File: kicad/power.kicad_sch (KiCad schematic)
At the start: 1 part, among them J1 1726480105

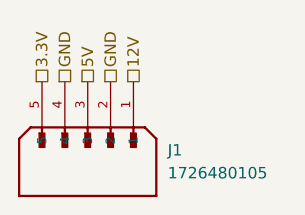
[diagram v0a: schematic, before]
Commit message: finished circuits for rp2040
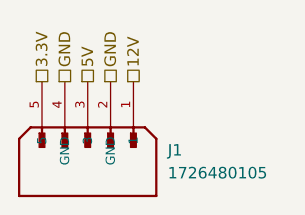
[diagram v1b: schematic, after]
